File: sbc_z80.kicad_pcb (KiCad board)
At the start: 4 copper layers, 102.6 x 50.8 mm, 92 parts, among them J1 RC80 Bus, J2 CTC Header, J3 AVR-JTAG-10, J4 IDE, J5 PIO Header, J6 Port A, J7 Port B, J8 USB_B_Micro, Q1 IRLML6402, SW1 Reset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

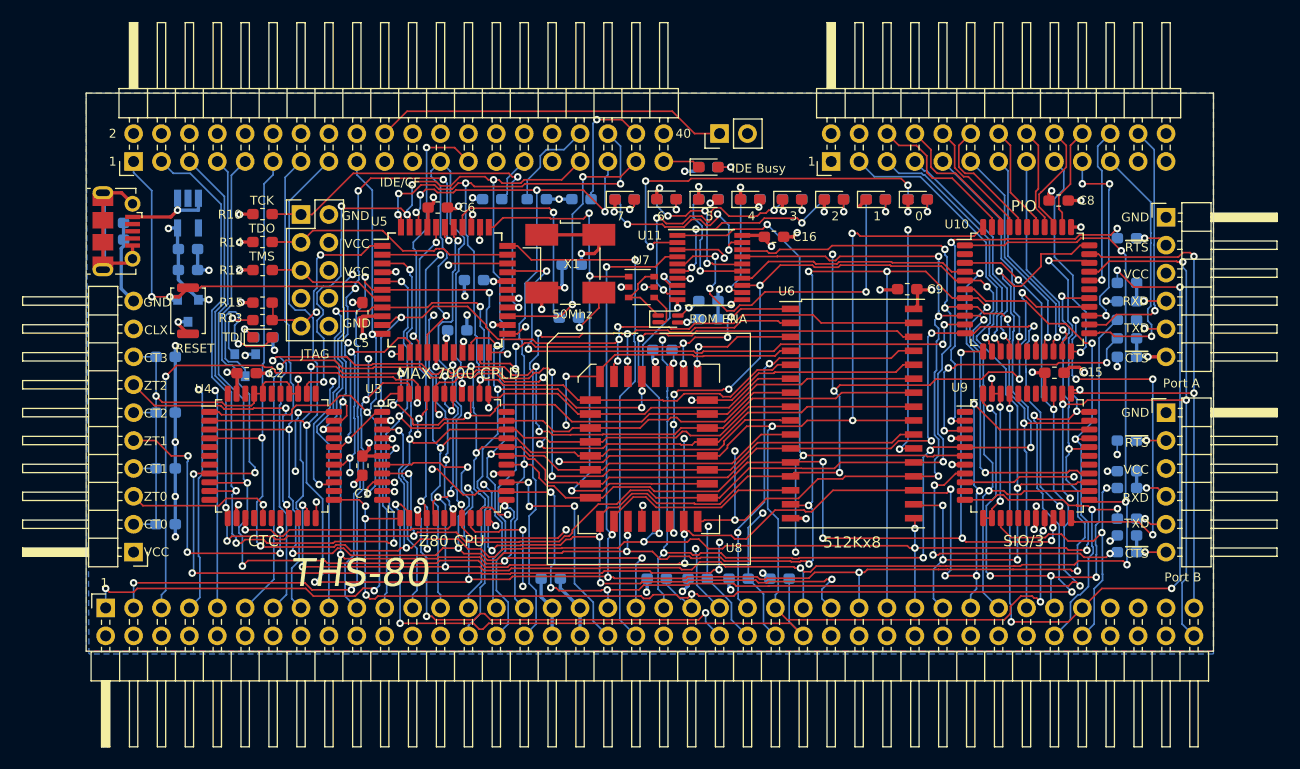
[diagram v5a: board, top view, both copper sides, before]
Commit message: fixed layout, added labels
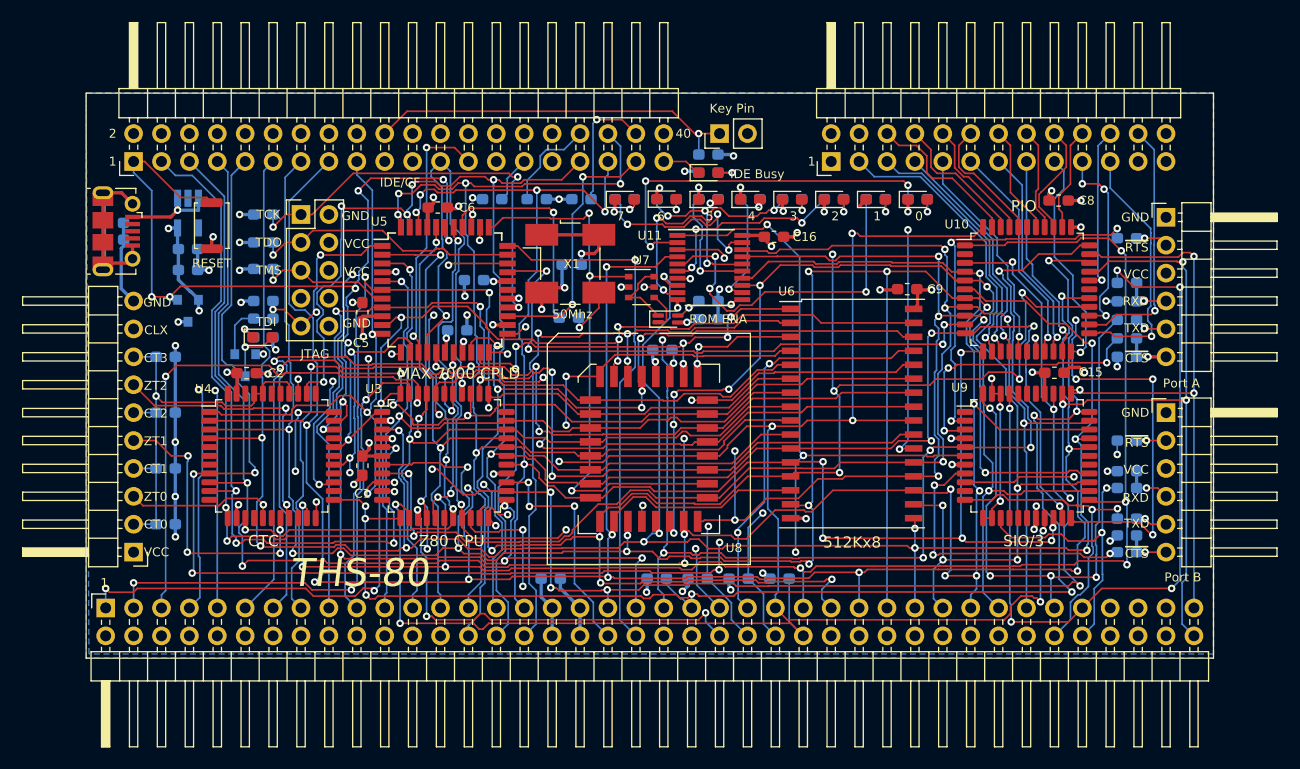
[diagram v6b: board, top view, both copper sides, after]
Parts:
- added C10: 100nF, Capacitor_SMD:C_0603_1608Metric_Pad1.05x0.95mm_HandSolder, B.Cu at (158.5, 87.4)
- R10, R12, R13, R14, R15: moved to B.Cu
- moved SW1 8.04 mm to (113.3, 93.9)
- moved R16 0.51 mm to (158.5, 89.0)
- moved D2 0.51 mm to (158.5, 89.0)
- moved R15 0.17 mm to (118.0, 100.7)
- moved R13 0.16 mm to (118.0, 102.3)
- moved R12 0.12 mm to (118.0, 97.8)
- moved R14 0.09 mm to (118.0, 95.4)
- moved R10 0.09 mm to (118.0, 92.8)
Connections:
- J1 pad 37: (no net) -> /USR1
- J1 pad 38: (no net) -> /USR2
- J1 pad 39: (no net) -> /USR3
- J1 pad 41: (no net) -> Net-(J1-Pad41)
- J1 pad 42: (no net) -> Net-(J1-Pad42)
- J1 pad 43: (no net) -> Net-(J1-Pad43)
- J1 pad 44: (no net) -> Net-(J1-Pad44)
- J1 pad 45: (no net) -> Net-(J1-Pad45)
- J1 pad 46: (no net) -> Net-(J1-Pad46)
- J1 pad 47: (no net) -> Net-(J1-Pad47)
- J1 pad 48: (no net) -> Net-(J1-Pad48)
- J1 pad 49: (no net) -> /A23
- J1 pad 50: (no net) -> /A22
- J1 pad 51: (no net) -> /A21
- J1 pad 52: (no net) -> /A20
- J1 pad 53: (no net) -> /A19
- J1 pad 61: (no net) -> /CLK2
- J1 pad 67: (no net) -> /D8
- J1 pad 68: (no net) -> /D9
- J1 pad 69: (no net) -> /D10
- J1 pad 70: (no net) -> /D11
- J1 pad 71: (no net) -> /D12
- J1 pad 72: (no net) -> /D13
- J1 pad 73: (no net) -> /D14
- J1 pad 74: (no net) -> /D15
- J1 pad 77: (no net) -> /USR5
- J1 pad 78: (no net) -> /USR6
- J1 pad 79: (no net) -> /USR7
- J2 pad 9: (no net) -> /CLKX
- J3 pad 7: (no net) -> Net-(J3-Pad7)
- J3 pad 8: (no net) -> Net-(J3-Pad8)
- J4 pad 10: (no net) -> Net-(J4-Pad10)
- J4 pad 12: (no net) -> Net-(J4-Pad12)
- J4 pad 14: (no net) -> Net-(J4-Pad14)
- J4 pad 16: (no net) -> Net-(J4-Pad16)
- J4 pad 18: (no net) -> Net-(J4-Pad18)
- J4 pad 21: (no net) -> Net-(J4-Pad21)
- J4 pad 27: (no net) -> Net-(J4-Pad27)
- J4 pad 28: (no net) -> Net-(J4-Pad28)
- J4 pad 31: (no net) -> Net-(J4-Pad31)
- J4 pad 32: (no net) -> Net-(J4-Pad32)
- J4 pad 4: (no net) -> Net-(J4-Pad4)
- J4 pad 6: (no net) -> Net-(J4-Pad6)
- J4 pad 8: (no net) -> Net-(J4-Pad8)
- J6 pad 3: (no net) -> Net-(J6-Pad3)
- J7 pad 3: (no net) -> Net-(J7-Pad3)
- J8 pad 2: (no net) -> Net-(J8-Pad2)
- J8 pad 3: (no net) -> Net-(J8-Pad3)
- J8 pad 4: (no net) -> Net-(J8-Pad4)
- U10 pad 2: (no net) -> Net-(U10-Pad2)
- U10 pad 28: (no net) -> Net-(U10-Pad28)
- U10 pad 39: (no net) -> Net-(U10-Pad39)
- U12 pad 4: (no net) -> Net-(U12-Pad4)
- U3 pad 11: (no net) -> Net-(U3-Pad11)
- U3 pad 17: (no net) -> Net-(U3-Pad17)
- U3 pad 33: (no net) -> Net-(U3-Pad33)
- U3 pad 39: (no net) -> Net-(U3-Pad39)
- U4 pad 11: (no net) -> Net-(U4-Pad11)
- U4 pad 15: (no net) -> Net-(U4-Pad15)
- U4 pad 17: (no net) -> Net-(U4-Pad17)
- U4 pad 20: (no net) -> Net-(U4-Pad20)
- U4 pad 24: (no net) -> Net-(U4-Pad24)
- U4 pad 26: (no net) -> Net-(U4-Pad26)
- U4 pad 28: (no net) -> Net-(U4-Pad28)
- U4 pad 30: (no net) -> Net-(U4-Pad30)
- U4 pad 34: (no net) -> Net-(U4-Pad34)
- U4 pad 38: (no net) -> Net-(U4-Pad38)
- U4 pad 39: (no net) -> Net-(U4-Pad39)
- U4 pad 42: (no net) -> Net-(U4-Pad42)
- U4 pad 44: (no net) -> Net-(U4-Pad44)
- U4 pad 5: (no net) -> Net-(U4-Pad5)
- U4 pad 6: (no net) -> Net-(U4-Pad6)
- U4 pad 7: (no net) -> Net-(U4-Pad7)
- U5 pad 28: (no net) -> /PIO_~RST~
- U9 pad 1: (no net) -> Net-(U9-Pad1)
- U9 pad 10: (no net) -> Net-(U9-Pad10)
- U9 pad 15: (no net) -> Net-(U9-Pad15)
- U9 pad 16: (no net) -> Net-(U9-Pad16)
- U9 pad 17: (no net) -> Net-(U9-Pad17)
- U9 pad 27: (no net) -> /DO
- U9 pad 28: (no net) -> Net-(U9-Pad28)
- U9 pad 38: (no net) -> Net-(U9-Pad38)
- U9 pad 39: (no net) -> Net-(U9-Pad39)
- U9 pad 40: (no net) -> Net-(U9-Pad40)
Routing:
- net /~RESET: track 192.8 -> 202.2 mm
- net Net-(D1-Pad2): track 14.7 -> 5.47 mm
- net Net-(C10-Pad1): track 32.2 -> 34.1 mm, vias 0 -> 1
- net /CLK_CPU: track 141.3 -> 139.5 mm
- net /TCK: track 36.7 -> 38.4 mm, vias 2 -> 3
- net /TDO: track 22.8 -> 24.5 mm, vias 0 -> 1
- net /TMS: track 10.3 -> 11.7 mm, vias 0 -> 1
- net GND: track 68.4 -> 69.7 mm, vias 40 -> 42
- net /TDI: track 17.1 -> 18.2 mm, vias 2 -> 3
- net Net-(Q1-Pad1): track 5.57 -> 4.61 mm, vias 1 -> 0
- net /~ACTIVE: track 2.86 -> 3.61 mm
- net /ARDY: track 18.6 -> 18.0 mm
- net /A9: track 95.6 -> 95.0 mm
- net Net-(R27-Pad1): track 9.20 -> 9.71 mm
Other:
- board size 102.6 x 50.8 mm -> 102.6 x 51.4 mm
- board text added: "Key Pin"
